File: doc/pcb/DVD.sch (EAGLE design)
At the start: 32 parts, among them IC1 7805, IC2 74HC14N

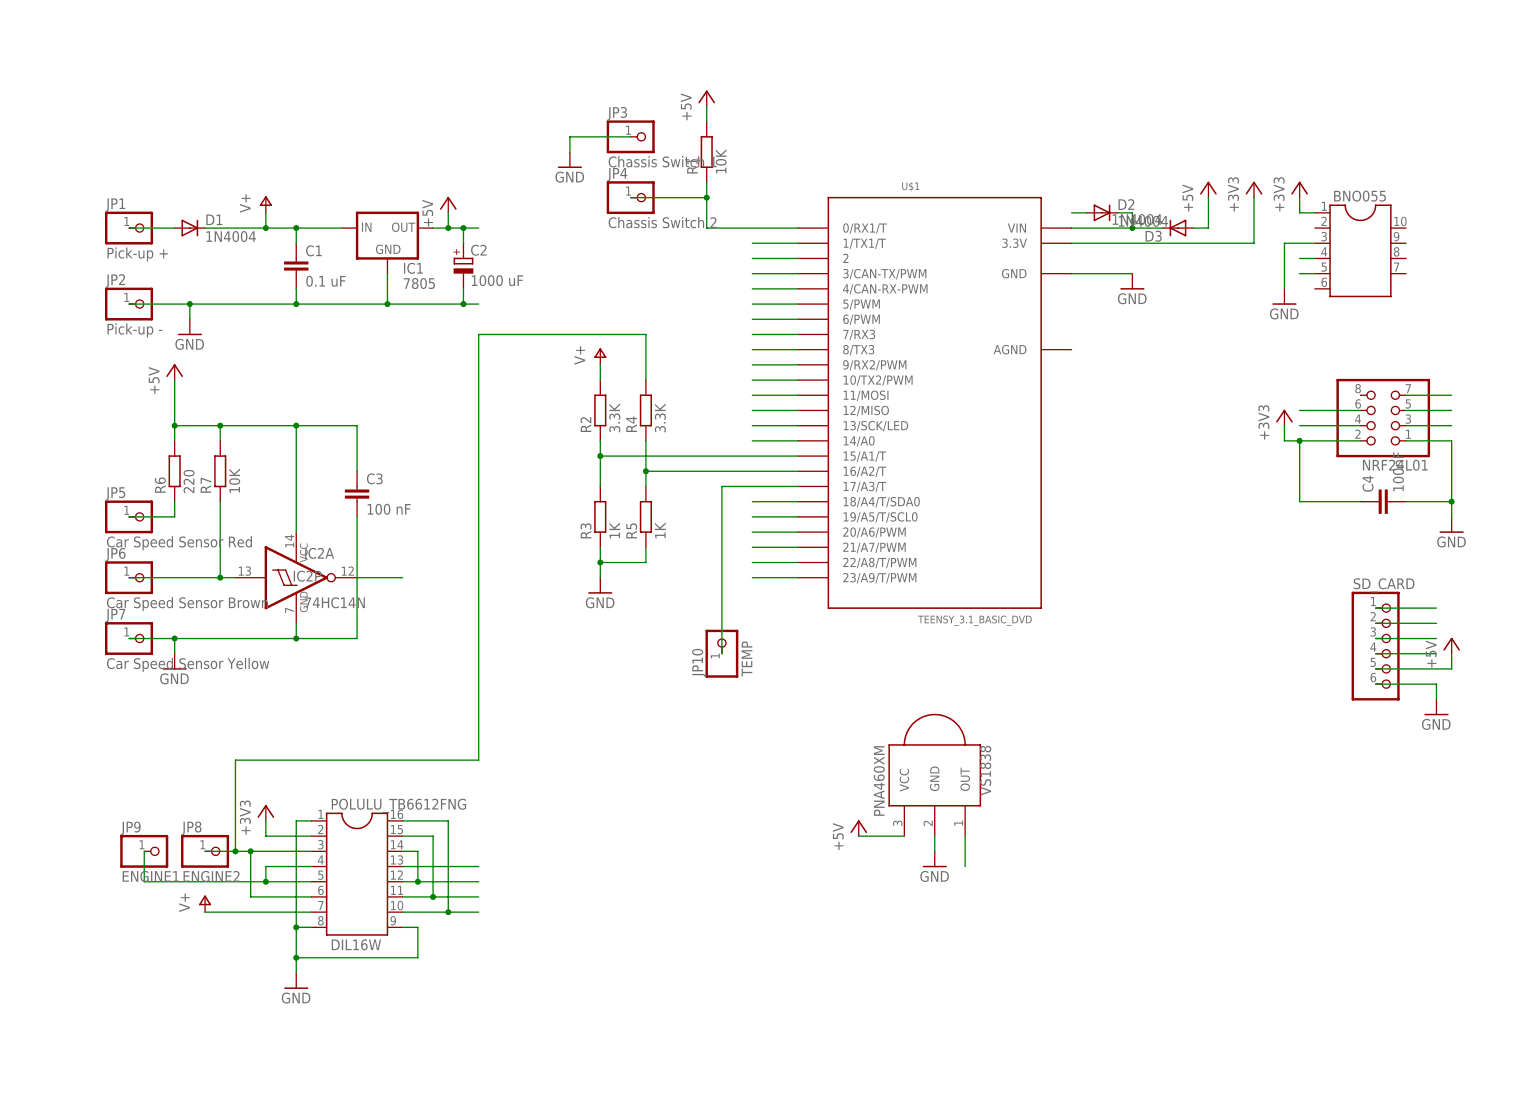
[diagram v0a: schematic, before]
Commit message: Created DVD.lbr for not existing parts and included them on PCB
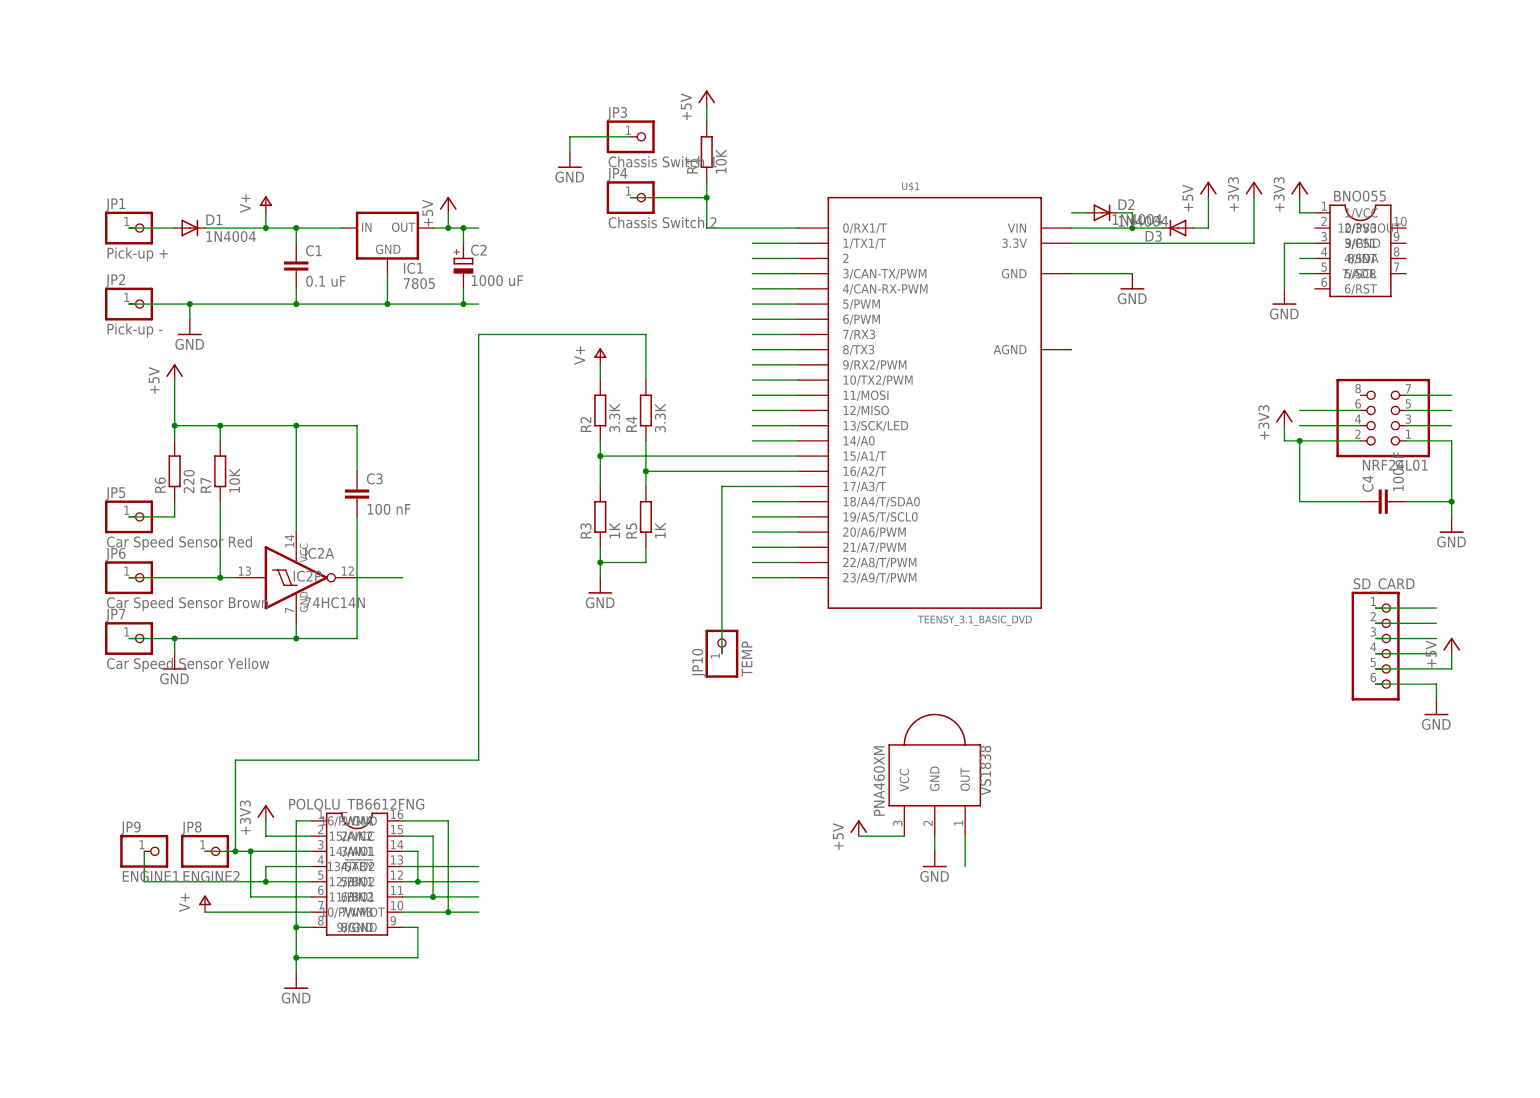
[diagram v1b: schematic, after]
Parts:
- removed BNO055: (no value), ic-package_mod:DIL10-6-4
- removed POLULU_TB6612FNG: DIL16W, ic-package_mod:DIL16W
- added U$2: POLOLU_TB6612FNG, DVD:POLOLU_TB6612FNG
- added U$4: BNO055, DVD:BNO055
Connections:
- net +3V3: now also U$2.2/VCC, U$4.1/VCC; no longer BNO055.1, POLULU_TB6612FNG.2
- net ENGINE1: now also U$2.4/AO2, U$2.5/BO2; no longer POLULU_TB6612FNG.4, POLULU_TB6612FNG.5
- net GND: now also U$2.1/GND, U$2.8/GND, U$2.9/GND, U$4.3/GND; no longer BNO055.3, POLULU_TB6612FNG.1, POLULU_TB6612FNG.8, POLULU_TB6612FNG.9
- net IN1: now also U$2.12/BIN1, U$2.14/AIN1; no longer POLULU_TB6612FNG.12, POLULU_TB6612FNG.14
- net IN2: now also U$2.11/BIN2, U$2.15/AIN2; no longer POLULU_TB6612FNG.11, POLULU_TB6612FNG.15
- net JP8: now also U$2.3/AO1, U$2.6/BO1; no longer POLULU_TB6612FNG.3, POLULU_TB6612FNG.6
- net PWM: now also U$2.10/PWMB, U$2.16/PWMA; no longer POLULU_TB6612FNG.10, POLULU_TB6612FNG.16
- net SCL: now also U$4.5/SCL; no longer BNO055.5
- net SDA: now also U$4.4/SDA; no longer BNO055.4
- net STBY: now also U$2.13/!STBY; no longer POLULU_TB6612FNG.13
- net V+: now also U$2.7/VMOT; no longer POLULU_TB6612FNG.7
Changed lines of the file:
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@@
 <part name="D2" library="adafruit" deviceset="1N4004" device=""/>
 <part name="D3" library="adafruit" deviceset="1N4004" device=""/>
-<part name="POLULU_TB6612FNG" library="ic-package_mod" deviceset="DIL16W" device="" value="DIL16W"/>
-<part name="BNO055" library="ic-package_mod" deviceset="DIL10-6-4" device=""/>
 <part name="U$1" library="Teensy_3_Series_Board_v1.0" deviceset="TEENSY_3.1_BASIC_DVD" device=""/>
+<part name="U$2" library="DVD" deviceset="POLOLU_TB6612FNG" device=""/>
+<part name="U$4" library="DVD" deviceset="BNO055" device=""/>
 </parts>
 <sheets>
@@
 <instance part="D2" gate="1" x="144.78" y="142.24"/>
 <instance part="D3" gate="1" x="157.48" y="139.7" rot="R180"/>
-<instance part="POLULU_TB6612FNG" gate="G$1" x="20.32" y="33.02"/>
-<instance part="BNO055" gate="G$1" x="187.96" y="137.16" rot="MR0"/>
 <instance part="U$1" gate="G$1" x="116.84" y="111.76"/>
+<instance part="U$2" gate="G$1" x="20.32" y="33.02"/>
+<instance part="U$4" gate="G$1" x="187.96" y="137.16" rot="MR0"/>
 </instances>
 <busses>
@@
 <wire x1="12.7" y1="25.4" x2="-5.08" y2="25.4" width="0.1524" layer="91"/>
 <pinref part="P+11" gate="1" pin="V+"/>
-<pinref part="POLULU_TB6612FNG" gate="G$1" pin="7"/>
+<pinref part="U$2" gate="G$1" pin="7/VMOT"/>
 </segment>
 <segment>
@@
 <wire x1="175.26" y1="137.16" x2="175.26" y2="129.54" width="0.1524" layer="91"/>
 <pinref part="GND12" gate="1" pin="GND"/>
-<pinref part="BNO055" gate="G$1" pin="3"/>
+<pinref part="U$4" gate="G$1" pin="3/GND"/>
 </segment>
 <segment>
@@
 <junction x="10.16" y="17.78"/>
 <pinref part="GND11" gate="1" pin="GND"/>
-<pinref part="POLULU_TB6612FNG" gate="G$1" pin="1"/>
-<pinref part="POLULU_TB6612FNG" gate="G$1" pin="8"/>
-<pinref part="POLULU_TB6612FNG" gate="G$1" pin="9"/>
+<pinref part="U$2" gate="G$1" pin="1/GND"/>
+<pinref part="U$2" gate="G$1" pin="8/GND"/>
+<pinref part="U$2" gate="G$1" pin="9/GND"/>
 </segment>
 </net>
@@
 <segment>
 <wire x1="27.94" y1="33.02" x2="40.64" y2="33.02" width="0.1524" layer="91"/>
-<pinref part="POLULU_TB6612FNG" gate="G$1" pin="13"/>
+<pinref part="U$2" gate="G$1" pin="13/!STBY"/>
 </segment>
 </net>
@@
 <wire x1="177.8" y1="142.24" x2="177.8" y2="144.78" width="0.1524" layer="91"/>
 <pinref part="+3V4" gate="G$1" pin="+3V3"/>
-<pinref part="BNO055" gate="G$1" pin="1"/>
+<pinref part="U$4" gate="G$1" pin="1/VCC"/>
 </segment>
 <segment>
@@
 <pinref part="+3V3" gate="G$1" pin="+3V3"/>
 <wire x1="5.08" y1="38.1" x2="5.08" y2="40.64" width="0.1524" layer="91"/>
-<pinref part="POLULU_TB6612FNG" gate="G$1" pin="2"/>
+<pinref part="U$2" gate="G$1" pin="2/VCC"/>
 </segment>
 </net>
@@
 <segment>
 <wire x1="180.34" y1="134.62" x2="177.8" y2="134.62" width="0.1524" layer="91"/>
-<pinref part="BNO055" gate="G$1" pin="4"/>
+<pinref part="U$4" gate="G$1" pin="4/SDA"/>
 </segment>
 <segment>
@@
 <segment>
 <wire x1="180.34" y1="132.08" x2="177.8" y2="132.08" width="0.1524" layer="91"/>
-<pinref part="BNO055" gate="G$1" pin="5"/>
+<pinref part="U$4" gate="G$1" pin="5/SCL"/>
 </segment>
 <segment>
@@
 <wire x1="0" y1="50.8" x2="0" y2="35.56" width="0.1524" layer="91"/>
 <junction x="0" y="35.56"/>
-<pinref part="POLULU_TB6612FNG" gate="G$1" pin="3"/>
-<pinref part="POLULU_TB6612FNG" gate="G$1" pin="6"/>
+<pinref part="U$2" gate="G$1" pin="3/AO1"/>
+<pinref part="U$2" gate="G$1" pin="6/BO1"/>
 </segment>
 </net>
@@
 <wire x1="-15.24" y1="30.48" x2="-15.24" y2="35.56" width="0.1524" layer="91"/>
 <junction x="5.08" y="30.48"/>
-<pinref part="POLULU_TB6612FNG" gate="G$1" pin="4"/>
-<pinref part="POLULU_TB6612FNG" gate="G$1" pin="5"/>
+<pinref part="U$2" gate="G$1" pin="4/AO2"/>
+<pinref part="U$2" gate="G$1" pin="5/BO2"/>
 </segment>
 </net>
@@
 <junction x="30.48" y="30.48"/>
 <wire x1="30.48" y1="30.48" x2="40.64" y2="30.48" width="0.1524" layer="91"/>
-<pinref part="POLULU_TB6612FNG" gate="G$1" pin="12"/>
-<pinref part="POLULU_TB6612FNG" gate="G$1" pin="14"/>
+<pinref part="U$2" gate="G$1" pin="12/BIN1"/>
+<pinref part="U$2" gate="G$1" pin="14/AIN1"/>
 </segment>
 <segment>
@@
 <junction x="33.02" y="27.94"/>
 <wire x1="33.02" y1="27.94" x2="40.64" y2="27.94" width="0.1524" layer="91"/>
-<pinref part="POLULU_TB6612FNG" gate="G$1" pin="11"/>
-<pinref part="POLULU_TB6612FNG" gate="G$1" pin="15"/>
+<pinref part="U$2" gate="G$1" pin="11/BIN2"/>
+<pinref part="U$2" gate="G$1" pin="15/AIN2"/>
 </segment>
 <segment>
@@
 <junction x="35.56" y="25.4"/>
 <wire x1="35.56" y1="25.4" x2="40.64" y2="25.4" width="0.1524" layer="91"/>
-<pinref part="POLULU_TB6612FNG" gate="G$1" pin="10"/>
-<pinref part="POLULU_TB6612FNG" gate="G$1" pin="16"/>
-</segment>
-<segment>
+<pinref part="U$2" gate="G$1" pin="10/PWMB"/>
+<pinref part="U$2" gate="G$1" pin="16/PWMA"/>
+</segment>
+<segment>

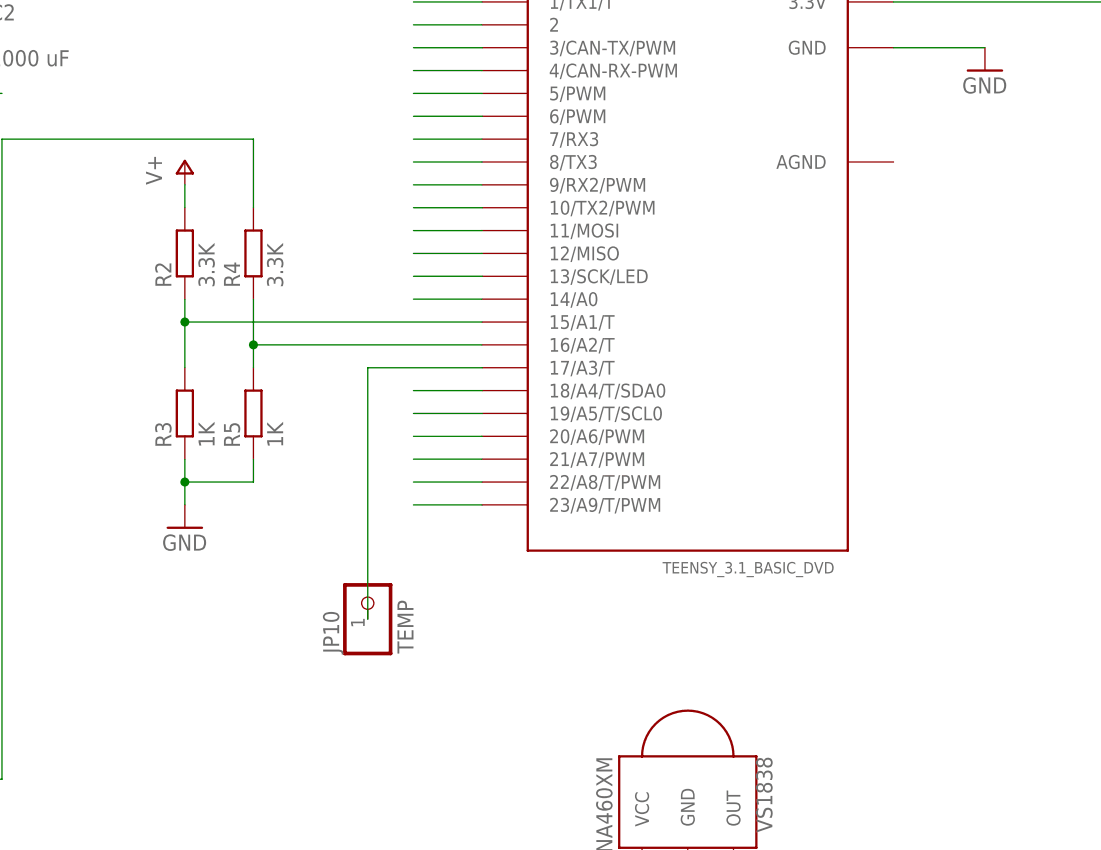
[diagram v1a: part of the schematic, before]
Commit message: PCB contacted Analog meas with AGND, removed temp meas
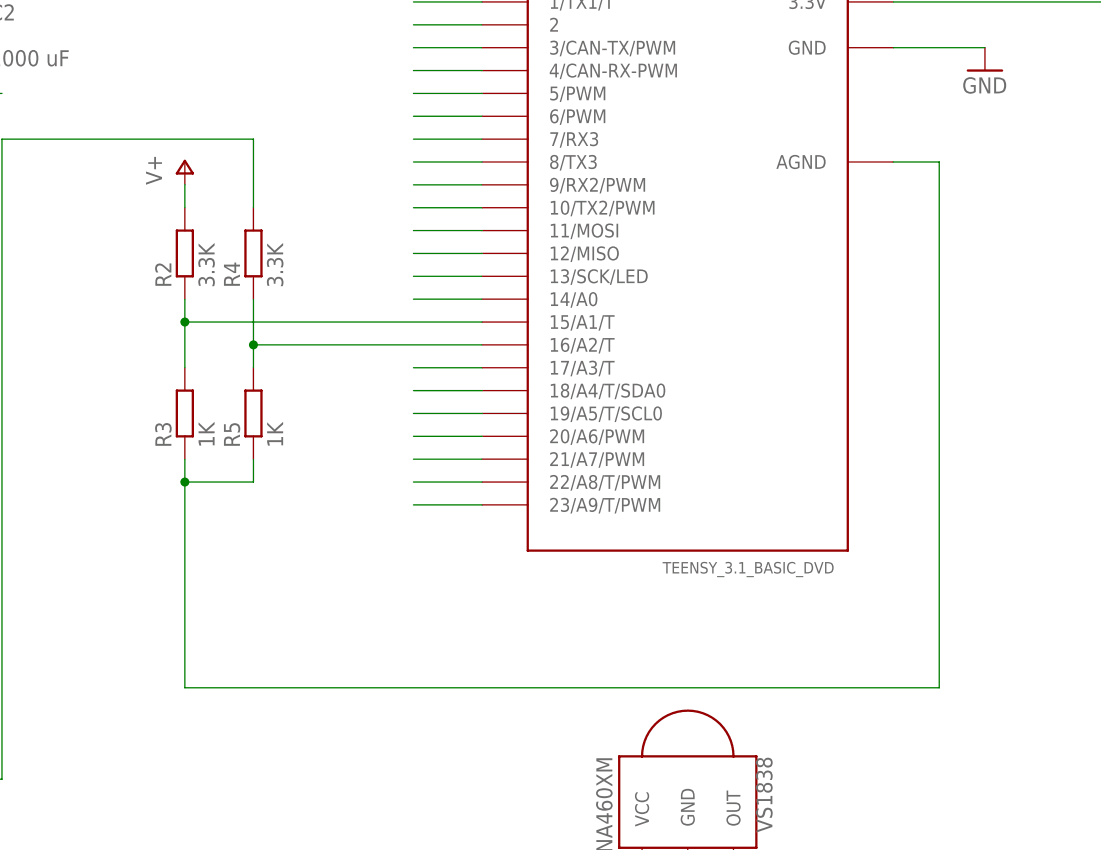
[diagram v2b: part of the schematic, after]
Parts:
- removed JP10: TEMP, pinhead:PINHD-1X1
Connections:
- removed net JP0: JP10.1, U$1.17/A3/T
- new net AGND: R3.1, R5.1, U$1.AGND
- new net N$6: U$1.17/A3/T
- net GND: no longer R3.1, R5.1
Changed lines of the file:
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@@
 <part name="GND3" library="supply1" deviceset="GND" device=""/>
 <part name="GND4" library="supply1" deviceset="GND" device=""/>
-<part name="GND5" library="supply1" deviceset="GND" device=""/>
 <part name="GND6" library="supply1" deviceset="GND" device=""/>
 <part name="GND7" library="supply1" deviceset="GND" device=""/>
@@
 <part name="C3" library="resistor" deviceset="C-EU" device="025-025X050" value="100 nF"/>
 <part name="C4" library="resistor" deviceset="C-EU" device="025-025X050" value="100nF"/>
-<part name="JP10" library="pinhead" deviceset="PINHD-1X1" device="" value="TEMP"/>
 <part name="D2" library="adafruit" deviceset="1N4004" device=""/>
 <part name="D3" library="adafruit" deviceset="1N4004" device=""/>
@@
 <instance part="GND3" gate="1" x="116.84" y="33.02"/>
 <instance part="GND4" gate="1" x="55.88" y="149.86"/>
-<instance part="GND5" gate="1" x="60.96" y="78.74"/>
 <instance part="GND6" gate="1" x="-10.16" y="66.04"/>
 <instance part="GND7" gate="1" x="200.66" y="58.42"/>
@@
 <instance part="C3" gate="G$1" x="20.32" y="96.52"/>
 <instance part="C4" gate="G$1" x="190.5" y="93.98" rot="R90"/>
-<instance part="JP10" gate="G$1" x="81.28" y="71.12" rot="R90"/>
 <instance part="D2" gate="1" x="144.78" y="142.24"/>
 <instance part="D3" gate="1" x="157.48" y="139.7" rot="R180"/>
@@
 </segment>
 <segment>
-<pinref part="GND5" gate="1" pin="GND"/>
-<pinref part="R3" gate="G$1" pin="1"/>
-<wire x1="60.96" y1="81.28" x2="60.96" y2="83.82" width="0.1524" layer="91"/>
-<pinref part="R5" gate="G$1" pin="1"/>
-<wire x1="60.96" y1="83.82" x2="60.96" y2="86.36" width="0.1524" layer="91"/>
-<wire x1="68.58" y1="86.36" x2="68.58" y2="83.82" width="0.1524" layer="91"/>
-<wire x1="68.58" y1="83.82" x2="60.96" y2="83.82" width="0.1524" layer="91"/>
-<junction x="60.96" y="83.82"/>
-</segment>
-<segment>
 <pinref part="GND6" gate="1" pin="GND"/>
 <wire x1="-10.16" y1="68.58" x2="-10.16" y2="71.12" width="0.1524" layer="91"/>
@@
 </segment>
 </net>
-<net name="JP0" class="0">
-<segment>
-<wire x1="93.98" y1="96.52" x2="81.28" y2="96.52" width="0.1524" layer="91"/>
-<pinref part="JP10" gate="G$1" pin="1"/>
-<wire x1="81.28" y1="68.58" x2="81.28" y2="96.52" width="0.1524" layer="91"/>
-<pinref part="U$1" gate="G$1" pin="17/A3/T"/>
-</segment>
-</net>
 <net name="STBY" class="0">
 <segment>
@@
 </segment>
 </net>
+<net name="AGND" class="0">
+<segment>
+<pinref part="U$1" gate="G$1" pin="AGND"/>
+<wire x1="139.7" y1="119.38" x2="144.78" y2="119.38" width="0.1524" layer="91"/>
+<pinref part="R3" gate="G$1" pin="1"/>
+<wire x1="60.96" y1="60.96" x2="60.96" y2="83.82" width="0.1524" layer="91"/>
+<pinref part="R5" gate="G$1" pin="1"/>
+<wire x1="60.96" y1="83.82" x2="60.96" y2="86.36" width="0.1524" layer="91"/>
+<wire x1="68.58" y1="86.36" x2="68.58" y2="83.82" width="0.1524" layer="91"/>
+<wire x1="68.58" y1="83.82" x2="60.96" y2="83.82" width="0.1524" layer="91"/>
+<junction x="60.96" y="83.82"/>
+<wire x1="60.96" y1="60.96" x2="144.78" y2="60.96" width="0.1524" layer="91"/>
+<wire x1="144.78" y1="60.96" x2="144.78" y2="119.38" width="0.1524" layer="91"/>
+</segment>
+</net>
+<net name="N$6" class="0">
+<segment>
+<pinref part="U$1" gate="G$1" pin="17/A3/T"/>
+<wire x1="93.98" y1="96.52" x2="86.36" y2="96.52" width="0.1524" layer="91"/>
+</segment>
+</net>
